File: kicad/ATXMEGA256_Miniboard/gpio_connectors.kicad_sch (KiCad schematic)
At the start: 6 parts, among them J10 2x5 Goldpin Socket, J11 2x5 Goldpin Socket, J12 2x3 Goldpin Socket, J13 2x5 Goldpin Socket, J14 2x5 Goldpin Socket, J9 2x5 Goldpin Socket

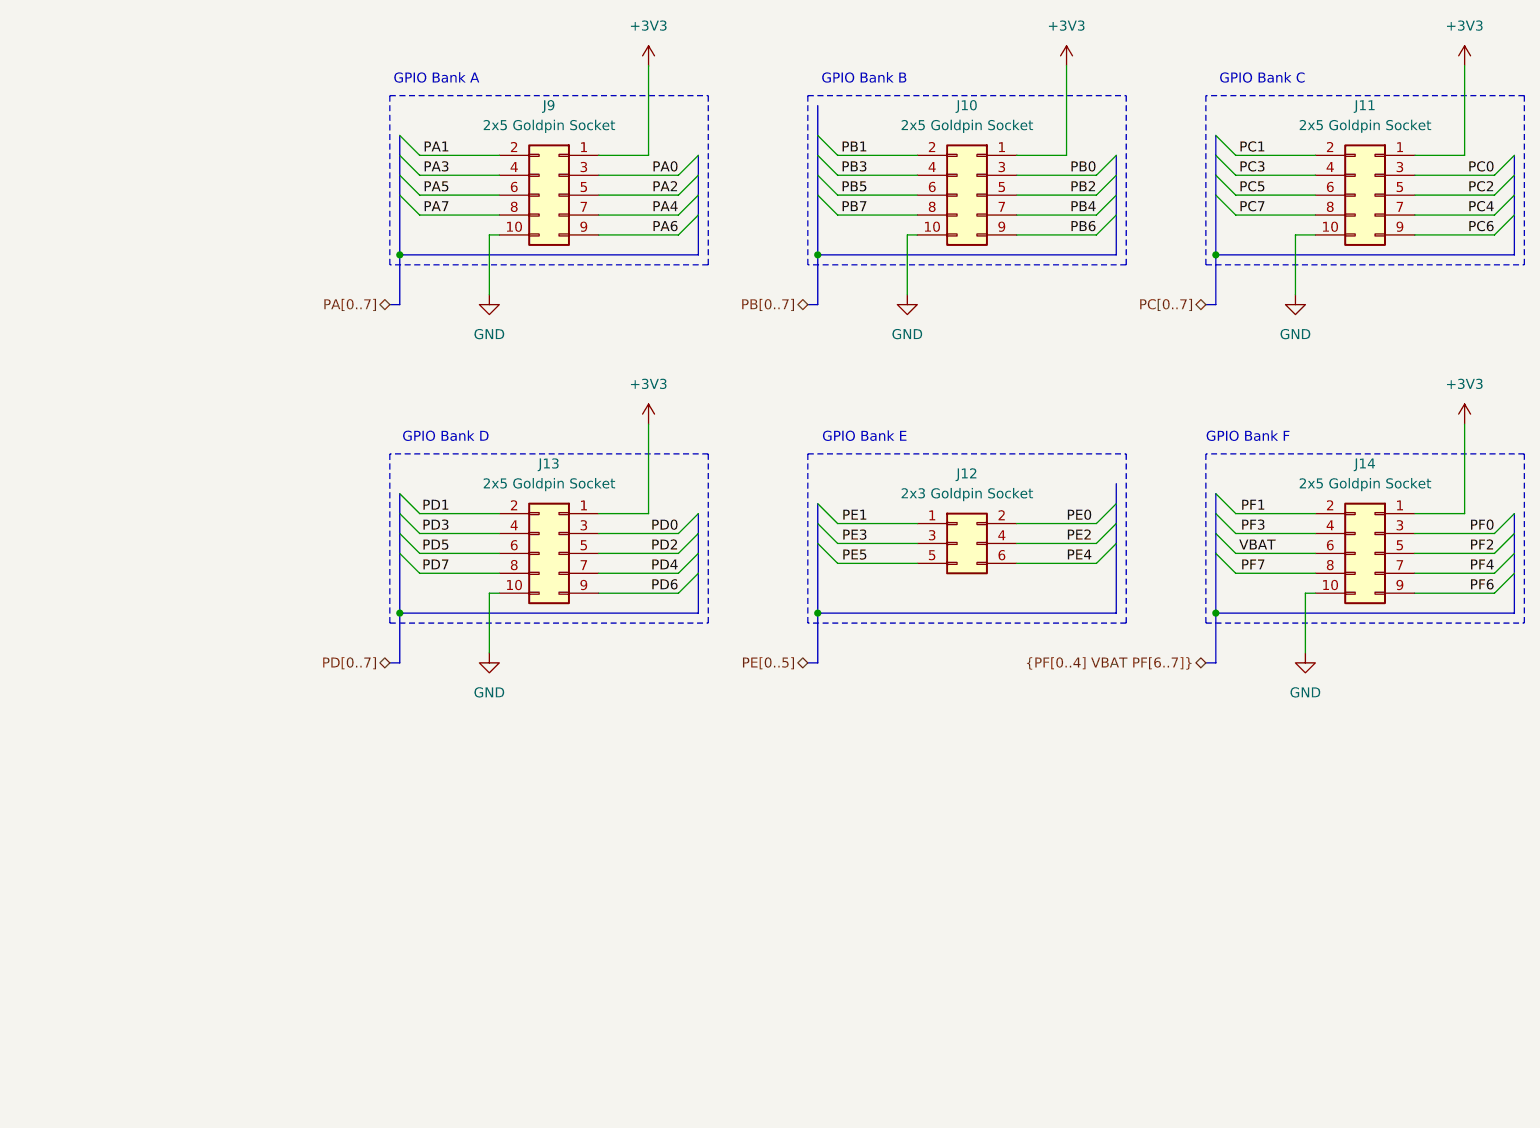
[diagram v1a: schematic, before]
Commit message: Poprawki zasilania, zmiana oscylatora RTC, poprawki polaczen GPIO
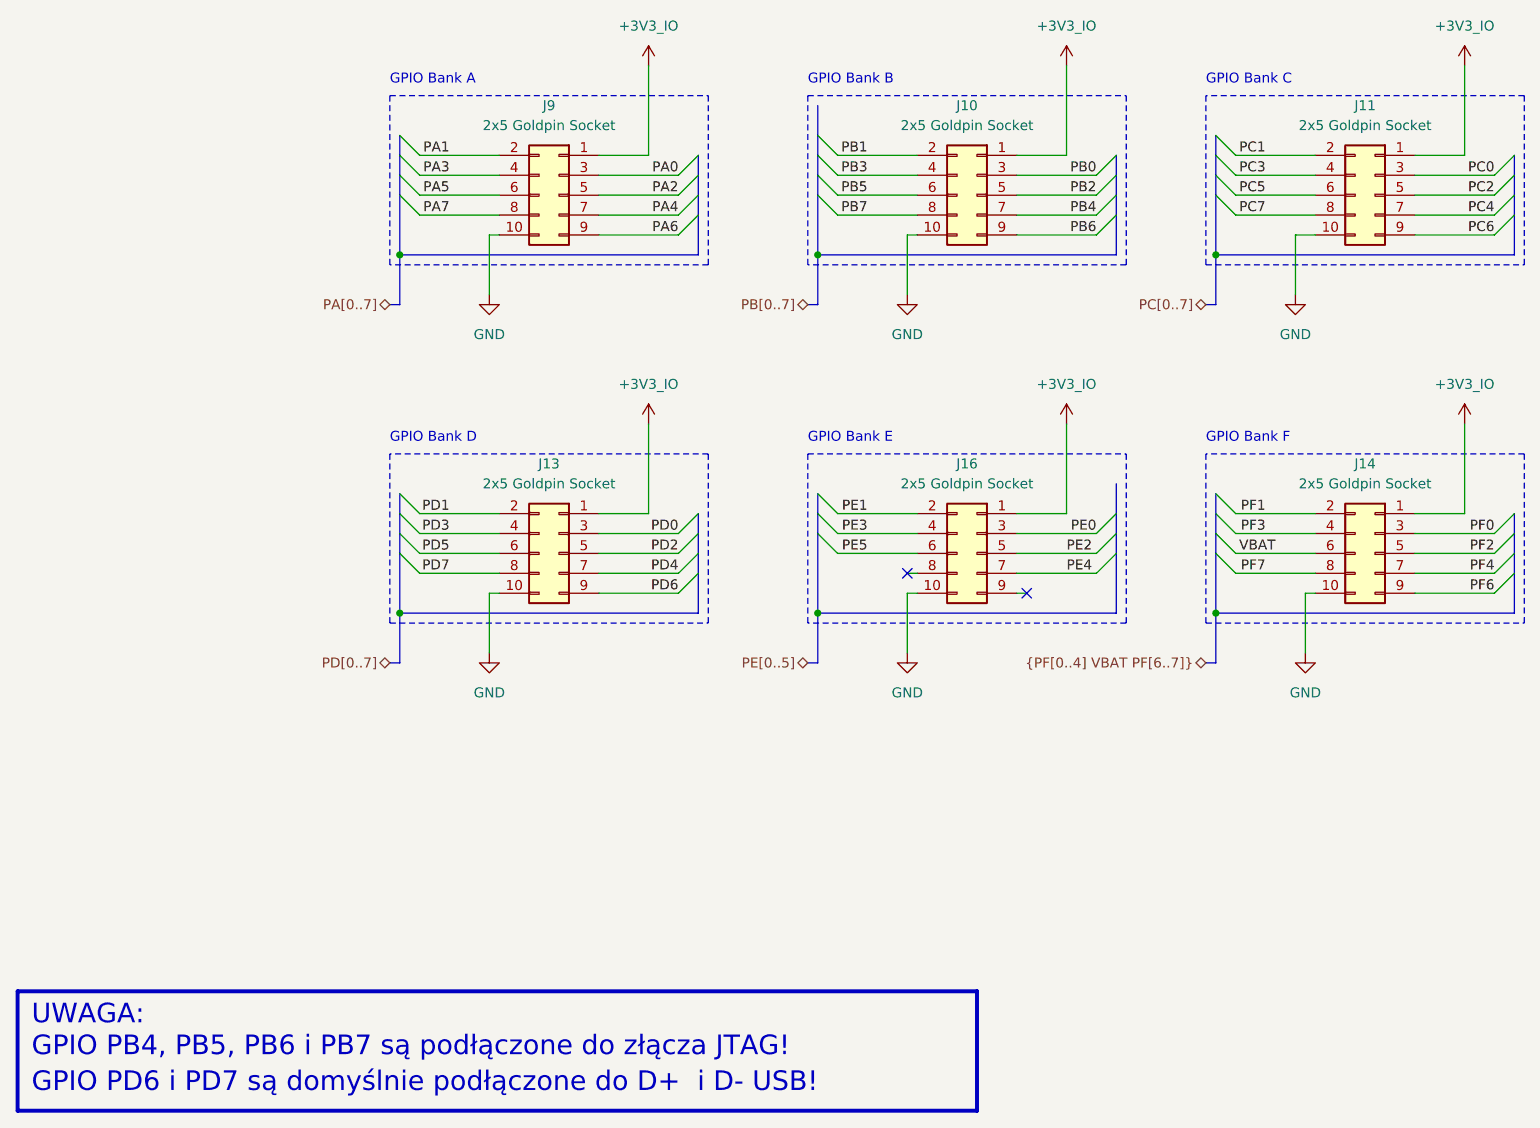
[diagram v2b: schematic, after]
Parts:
- removed J12: 2x3 Goldpin Socket, Connector_PinSocket_2.54mm:PinSocket_2x03_P2.54mm_Vertical_SMD, symbol Connector_Generic:Conn_02x03_Odd_Even
- added J16: 2x5 Goldpin Socket, Connector_PinSocket_2.54mm:PinSocket_2x05_P2.54mm_Vertical_SMD, symbol Connector_Generic:Conn_02x05_Odd_Even
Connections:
- net GND: now also J16.10 (Pin_10)
- net PE0: now also J16.3 (Pin_3)
- net PE1: now also J16.2 (Pin_2)
- net PE2: now also J16.5 (Pin_5)
- net PE3: now also J16.4 (Pin_4)
- net PE4: now also J16.7 (Pin_7)
- net PE5: now also J16.6 (Pin_6)
- net +3V3 renamed +3V3_IO
- net +3V3_IO: now also J16.1 (Pin_1)
- no-connect marks 0 -> 2
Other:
- note added: "GPIO PB4, PB5, PB6 i PB7 są podłączone do złącza JTAG!"
- note added: "GPIO PD6 i PD7 są domyślnie podłączone do D+ i D- USB!"
- note added: "UWAGA:"

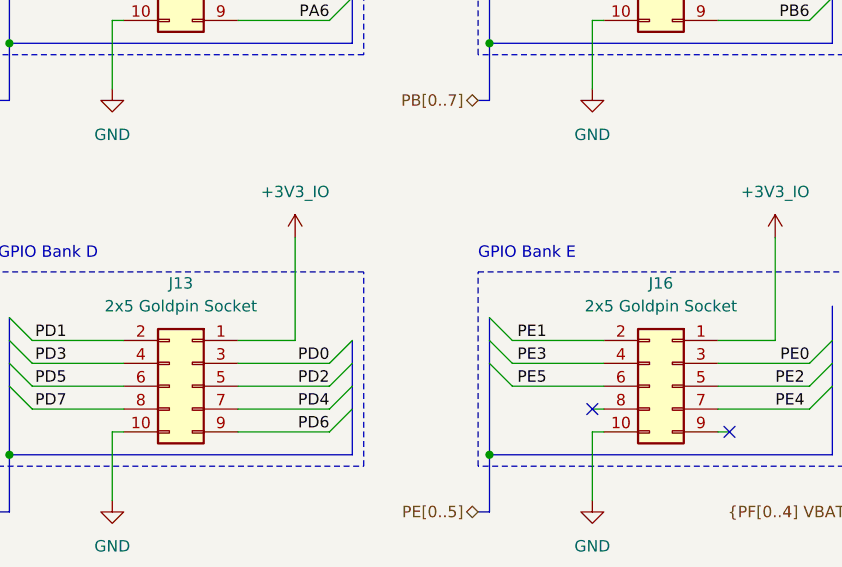
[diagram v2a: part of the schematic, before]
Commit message: Zmiana zlacza PDI, dodany makefile i struktura plikow
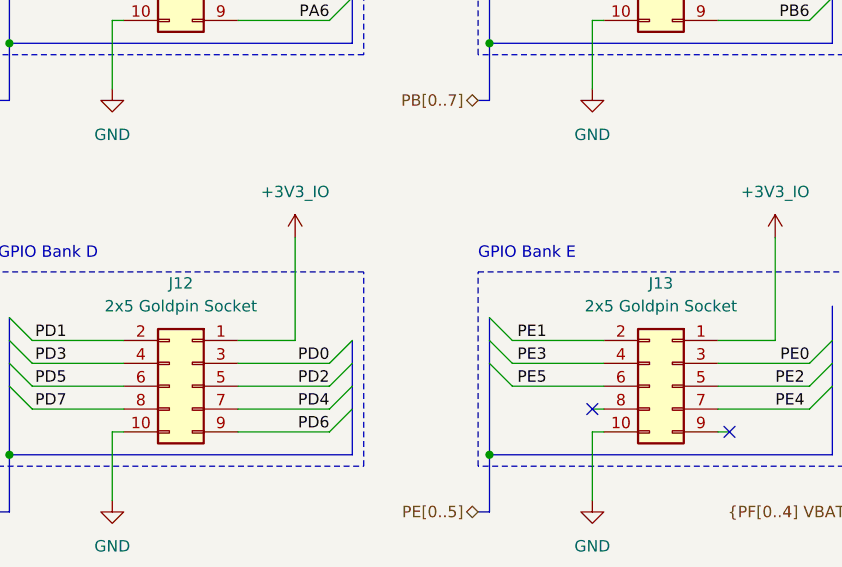
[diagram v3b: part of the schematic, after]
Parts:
- renumbered J13 to J12, J16 to J13
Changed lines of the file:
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@@
 		(on_board yes)
 		(dnp no)
-		(property "Reference" "J16"
+		(property "Reference" "J13"
 			(at 149.86 101.6 0)
 			(effects
@@
 			(project "ATXMEGA256_Miniboard"
 				(path "/ef1e5883-c6cf-4bad-8eaa-8ec9109f9d71/310cf5a3-b597-43ba-9125-314fa4b04872"
-					(reference "J16")
+					(reference "J13")
 					(unit 1)
 				)
@@
 		(dnp no)
 		(fields_autoplaced yes)
-		(property "Reference" "#PWR039"
+		(property "Reference" "#PWR033"
 			(at 109.22 100.33 0)
 			(effects
@@
 			(project "ATXMEGA256_Miniboard"
 				(path "/ef1e5883-c6cf-4bad-8eaa-8ec9109f9d71/310cf5a3-b597-43ba-9125-314fa4b04872"
-					(reference "#PWR039")
+					(reference "#PWR033")
 					(unit 1)
 				)
@@
 		(dnp no)
 		(fields_autoplaced yes)
-		(property "Reference" "#PWR028"
+		(property "Reference" "#PWR031"
 			(at 142.24 86.36 0)
 			(effects
@@
 			(project "ATXMEGA256_Miniboard"
 				(path "/ef1e5883-c6cf-4bad-8eaa-8ec9109f9d71/310cf5a3-b597-43ba-9125-314fa4b04872"
-					(reference "#PWR028")
+					(reference "#PWR031")
 					(unit 1)
 				)
@@
 		(dnp no)
 		(fields_autoplaced yes)
-		(property "Reference" "#PWR044"
+		(property "Reference" "#PWR028"
 			(at 162.56 54.61 0)
 			(effects
@@
 			(project "ATXMEGA256_Miniboard"
 				(path "/ef1e5883-c6cf-4bad-8eaa-8ec9109f9d71/310cf5a3-b597-43ba-9125-314fa4b04872"
-					(reference "#PWR044")
+					(reference "#PWR028")
 					(unit 1)
 				)
@@
 		(dnp no)
 		(fields_autoplaced yes)
-		(property "Reference" "#PWR029"
+		(property "Reference" "#PWR032"
 			(at 191.77 86.36 0)
 			(effects
@@
 			(project "ATXMEGA256_Miniboard"
 				(path "/ef1e5883-c6cf-4bad-8eaa-8ec9109f9d71/310cf5a3-b597-43ba-9125-314fa4b04872"
-					(reference "#PWR029")
+					(reference "#PWR032")
 					(unit 1)
 				)
@@
 		(dnp no)
 		(fields_autoplaced yes)
-		(property "Reference" "#PWR046"
+		(property "Reference" "#PWR035"
 			(at 213.36 100.33 0)
 			(effects
@@
 			(project "ATXMEGA256_Miniboard"
 				(path "/ef1e5883-c6cf-4bad-8eaa-8ec9109f9d71/310cf5a3-b597-43ba-9125-314fa4b04872"
-					(reference "#PWR046")
+					(reference "#PWR035")
 					(unit 1)
 				)
@@
 		(dnp no)
 		(fields_autoplaced yes)
-		(property "Reference" "#PWR032"
+		(property "Reference" "#PWR036"
 			(at 88.9 132.08 0)
 			(effects
@@
 			(project "ATXMEGA256_Miniboard"
 				(path "/ef1e5883-c6cf-4bad-8eaa-8ec9109f9d71/310cf5a3-b597-43ba-9125-314fa4b04872"
-					(reference "#PWR032")
+					(reference "#PWR036")
 					(unit 1)
 				)
@@
 		(dnp no)
 		(fields_autoplaced yes)
-		(property "Reference" "#PWR027"
+		(property "Reference" "#PWR030"
 			(at 88.9 86.36 0)
 			(effects
@@
 			(project "ATXMEGA256_Miniboard"
 				(path "/ef1e5883-c6cf-4bad-8eaa-8ec9109f9d71/310cf5a3-b597-43ba-9125-314fa4b04872"
-					(reference "#PWR027")
+					(reference "#PWR030")
 					(unit 1)
 				)
@@
 		(dnp no)
 		(fields_autoplaced yes)
-		(property "Reference" "#PWR045"
+		(property "Reference" "#PWR029"
 			(at 213.36 54.61 0)
 			(effects
@@
 			(project "ATXMEGA256_Miniboard"
 				(path "/ef1e5883-c6cf-4bad-8eaa-8ec9109f9d71/310cf5a3-b597-43ba-9125-314fa4b04872"
-					(reference "#PWR045")
+					(reference "#PWR029")
 					(unit 1)
 				)
@@
 		(dnp no)
 		(fields_autoplaced yes)
-		(property "Reference" "#PWR040"
+		(property "Reference" "#PWR027"
 			(at 109.22 54.61 0)
 			(effects
@@
 			(project "ATXMEGA256_Miniboard"
 				(path "/ef1e5883-c6cf-4bad-8eaa-8ec9109f9d71/310cf5a3-b597-43ba-9125-314fa4b04872"
-					(reference "#PWR040")
+					(reference "#PWR027")
 					(unit 1)
 				)
@@
 		(dnp no)
 		(fields_autoplaced yes)
-		(property "Reference" "#PWR033"
+		(property "Reference" "#PWR038"
 			(at 193.04 132.08 0)
 			(effects
@@
 			(project "ATXMEGA256_Miniboard"
 				(path "/ef1e5883-c6cf-4bad-8eaa-8ec9109f9d71/310cf5a3-b597-43ba-9125-314fa4b04872"
-					(reference "#PWR033")
+					(reference "#PWR038")
 					(unit 1)
 				)
@@
 		(on_board yes)
 		(dnp no)
-		(property "Reference" "J13"
+		(property "Reference" "J12"
 			(at 96.52 101.6 0)
 			(effects
@@
 			(project "ATXMEGA256_Miniboard"
 				(path "/ef1e5883-c6cf-4bad-8eaa-8ec9109f9d71/310cf5a3-b597-43ba-9125-314fa4b04872"
-					(reference "J13")
+					(reference "J12")
 					(unit 1)
 				)
@@
 		(dnp no)
 		(fields_autoplaced yes)
-		(property "Reference" "#PWR047"
+		(property "Reference" "#PWR034"
 			(at 162.56 100.33 0)
 			(effects
@@
 			(project "ATXMEGA256_Miniboard"
 				(path "/ef1e5883-c6cf-4bad-8eaa-8ec9109f9d71/310cf5a3-b597-43ba-9125-314fa4b04872"
-					(reference "#PWR047")
+					(reference "#PWR034")
 					(unit 1)
 				)
@@
 		(dnp no)
 		(fields_autoplaced yes)
-		(property "Reference" "#PWR048"
+		(property "Reference" "#PWR037"
 			(at 142.24 132.08 0)
 			(effects
@@
 			(project "ATXMEGA256_Miniboard"
 				(path "/ef1e5883-c6cf-4bad-8eaa-8ec9109f9d71/310cf5a3-b597-43ba-9125-314fa4b04872"
-					(reference "#PWR048")
-					(unit 1)
-				)
+					(reference "#PWR037")
+					(unit 1)
+				)

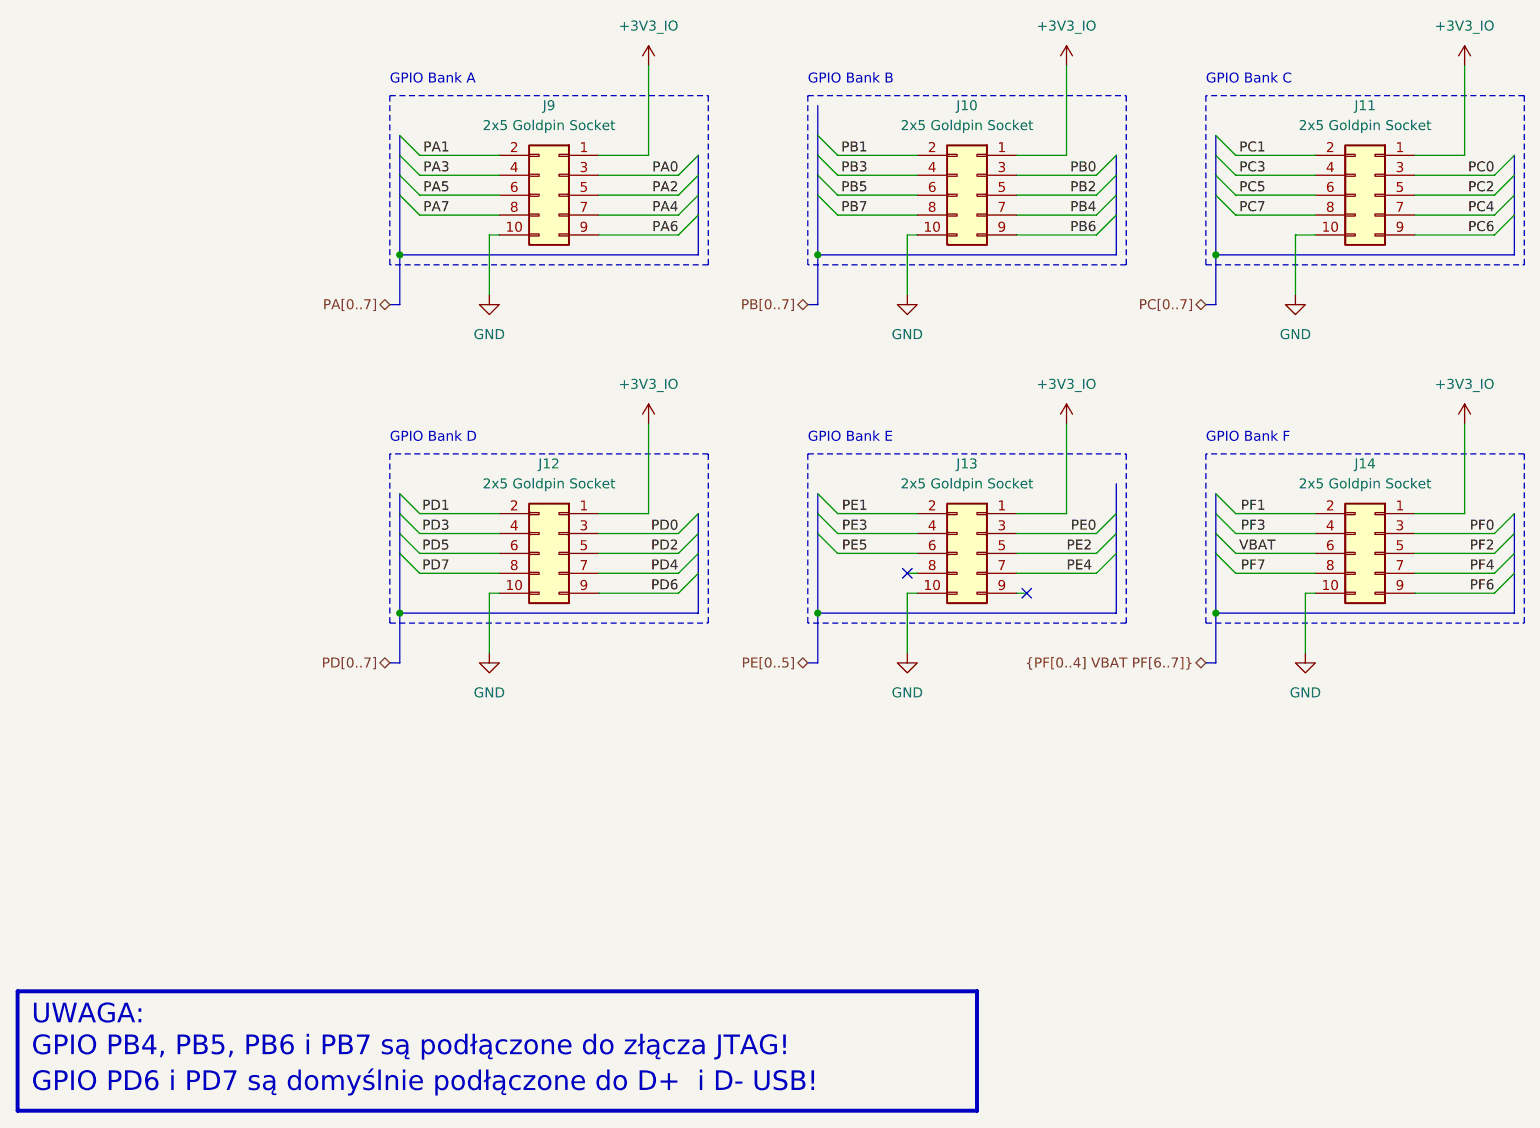
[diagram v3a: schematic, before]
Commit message: layout komponentów
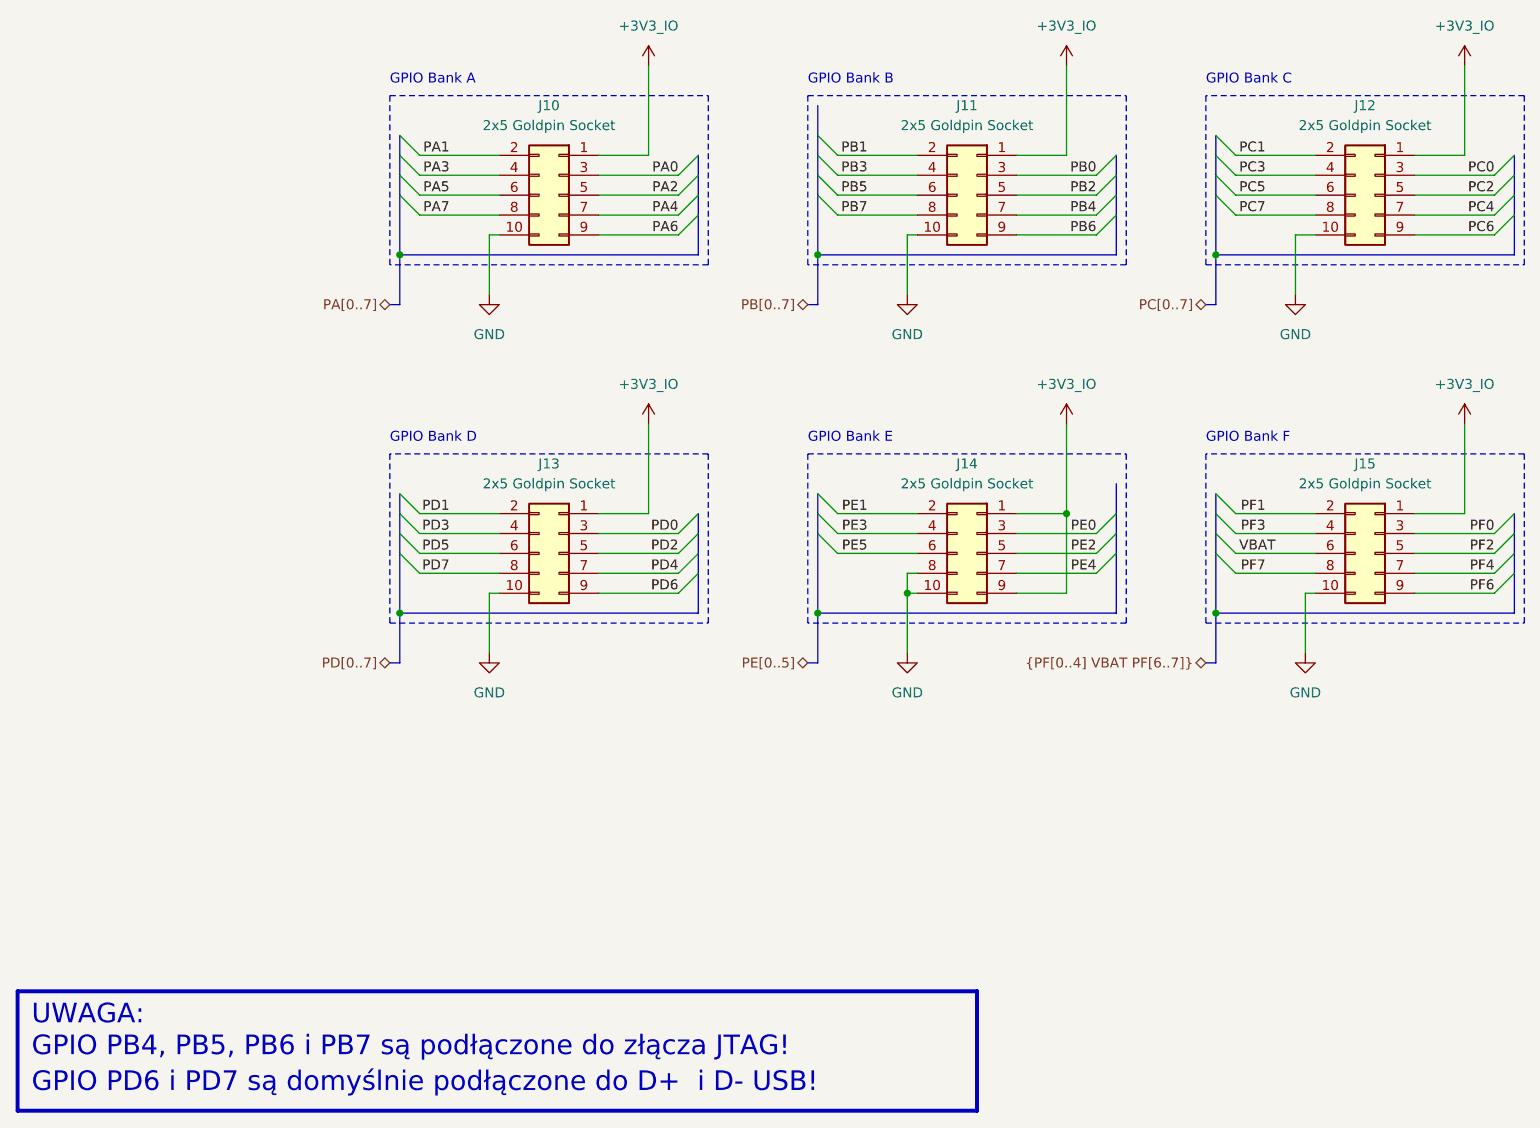
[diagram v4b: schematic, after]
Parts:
- renumbered J9 to J10, J10 to J11, J11 to J12, J12 to J13, J13 to J14, J14 to J15
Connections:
- net +3V3_IO: now also J14.9 (Pin_9)
- net GND: now also J14.8 (Pin_8)
- no-connect marks 2 -> 0
